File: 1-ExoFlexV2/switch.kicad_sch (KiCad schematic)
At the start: 40 parts, among them J20 SWMAX1, J21 SWMIN1, J22 SWMAX2, J23 SWMIN2, J24 SWMAX3, J25 SWMIN3, J26 SWMAX4, J27 SWMAX5, J28 URG1, J29 RESET

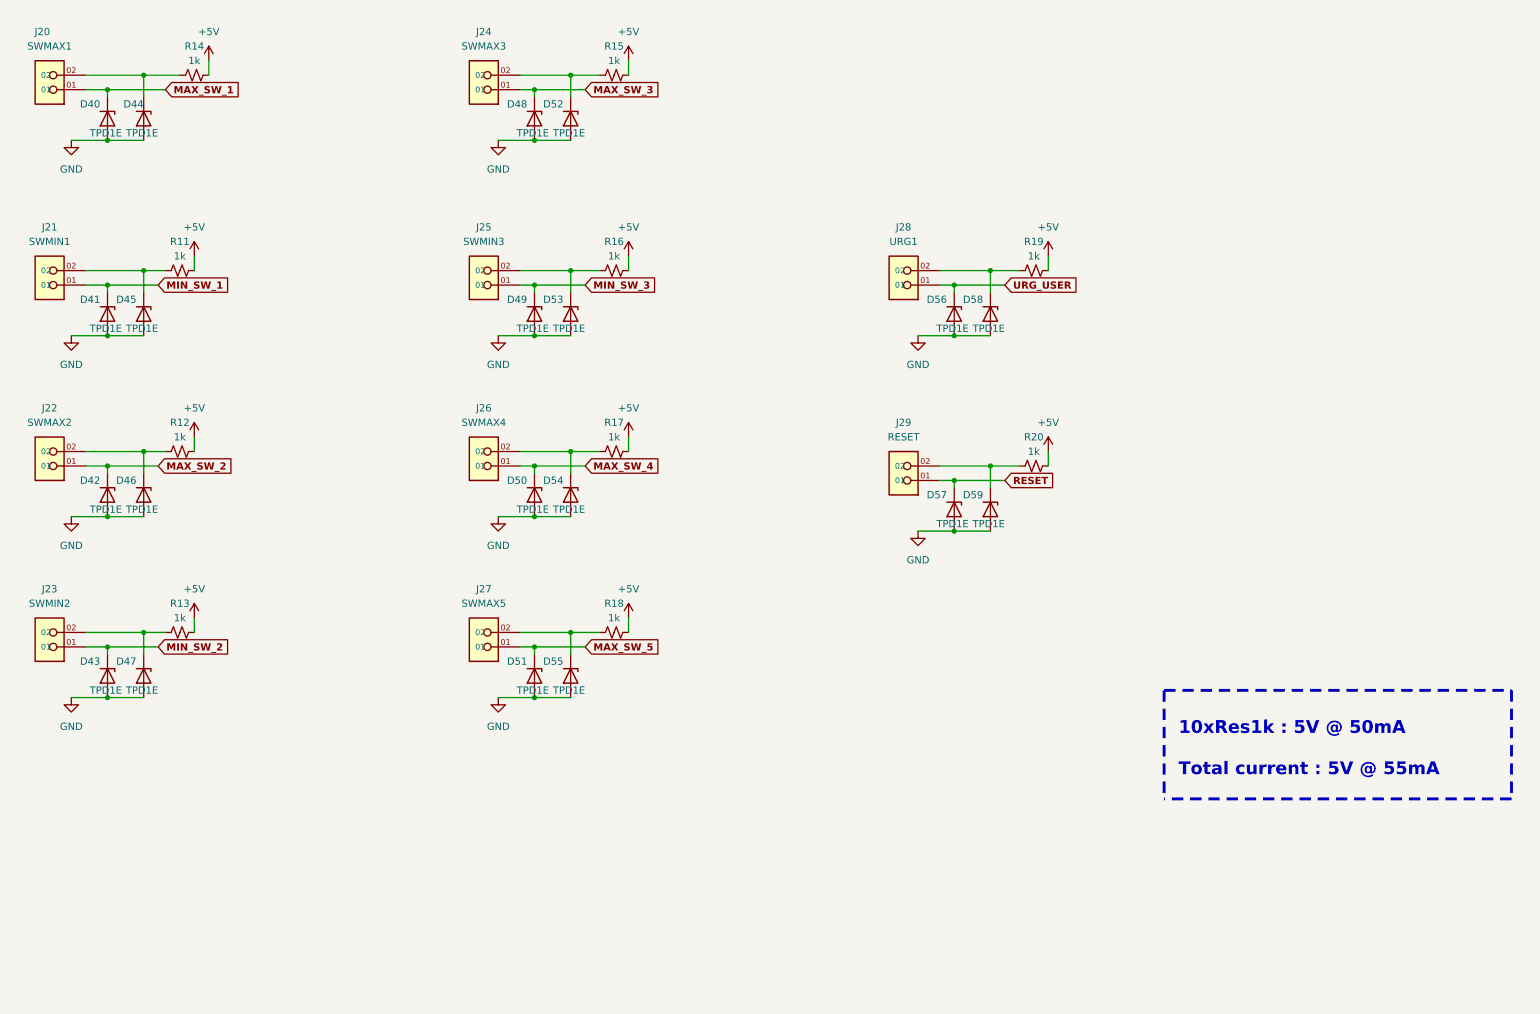
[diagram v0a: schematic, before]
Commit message: Trimmer et jumper
-Changement de symbole de jumper
-Ajout des des trimmer aux endroits nécessaires
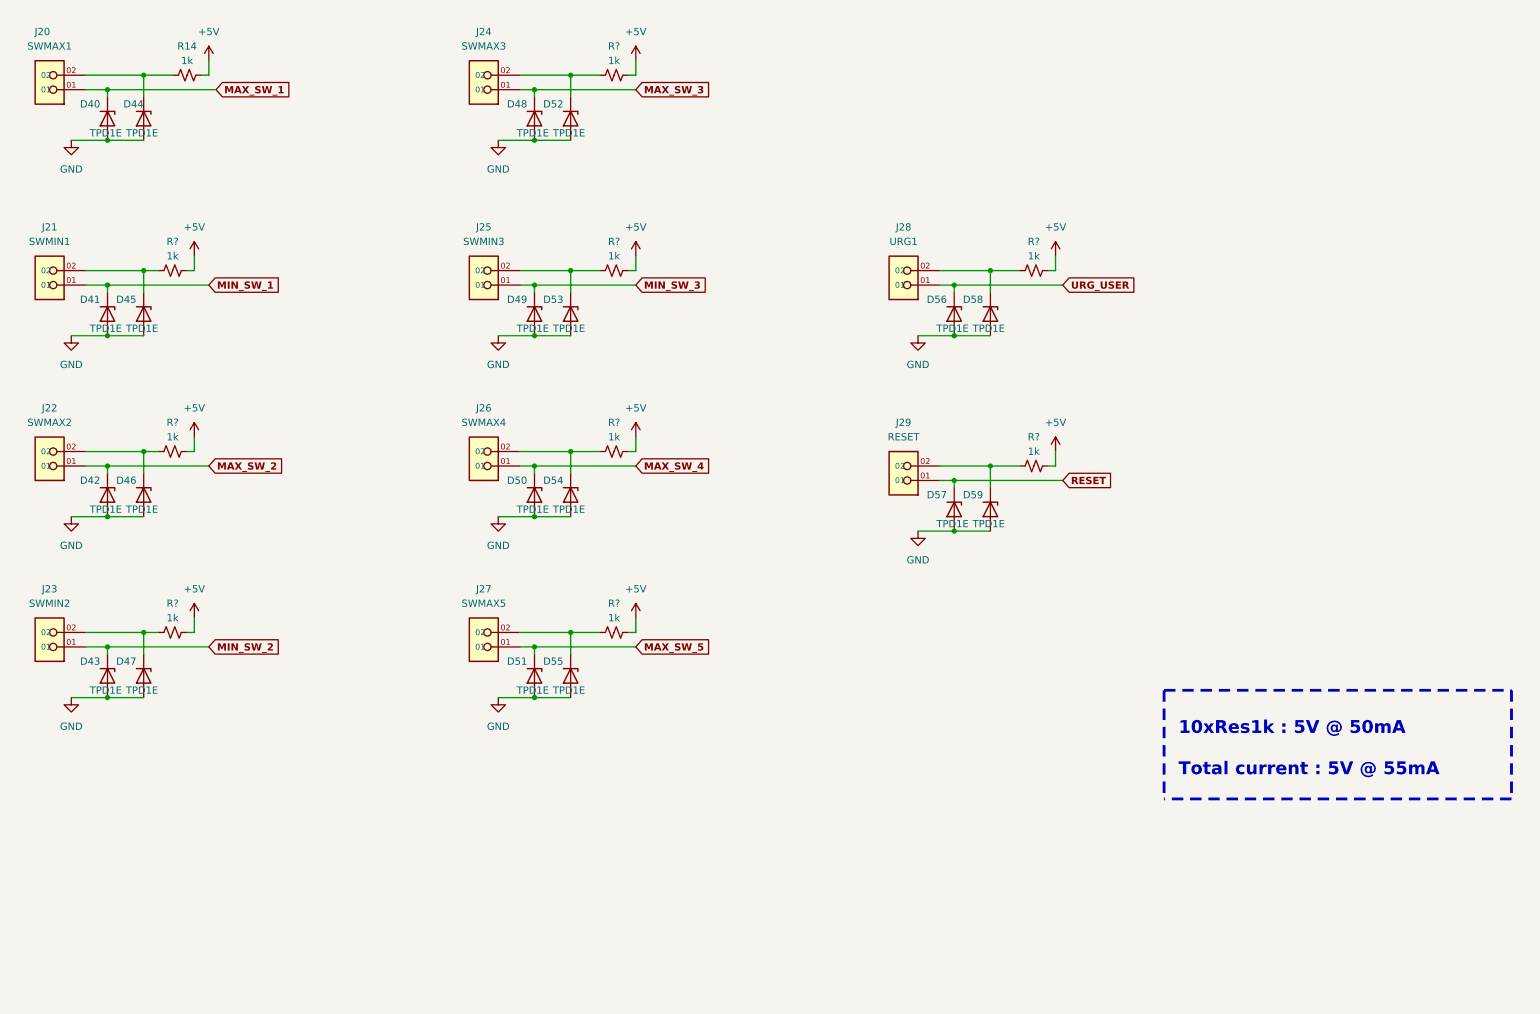
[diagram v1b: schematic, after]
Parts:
- removed R11, R12, R13, R15, R16, R17, R18, R19, R20: 1k, Resistor_SMD:R_0603_1608Metric, symbol Device:R_Small_US
- added R? (x9): 1k, Resistor_SMD:R_0805_2012Metric, symbol Device:R_Small_US
- R14: footprint Resistor_SMD:R_0603_1608Metric -> Resistor_SMD:R_0805_2012Metric
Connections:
- net +5V: now also R?.2, R?.2, R?.2, R?.2, R?.2, R?.2, R?.2, R?.2, R?.2
- net at D53.1 (K), J25.02: now also R?.1
- net at D59.1 (K), J29.02: now also R?.1
- net at D45.1 (K), J21.02: now also R?.1
- net at D47.1 (K), J23.02: now also R?.1
- net at D52.1 (K), J24.02: now also R?.1
- net at D54.1 (K), J26.02: now also R?.1
- net at D58.1 (K), J28.02: now also R?.1
- net at D46.1 (K), J22.02: now also R?.1
- net at D55.1 (K), J27.02: now also R?.1
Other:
- moved on the sheet: R14

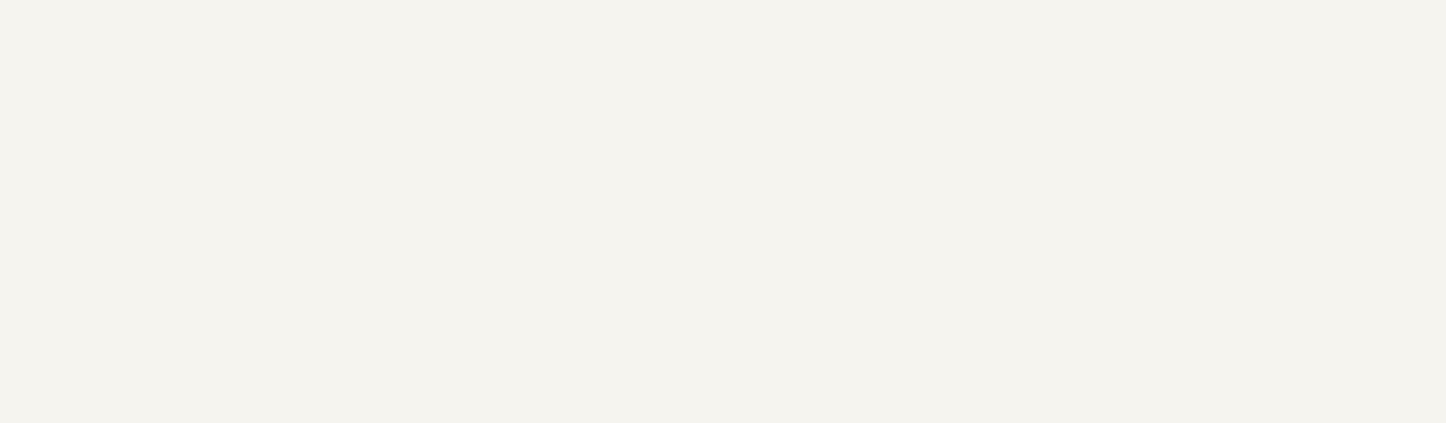
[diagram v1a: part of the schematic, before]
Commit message: Test points et notes
- Ajout de tous les tests point nécessaires
-  Ajoute des sections de notes dans chaque page
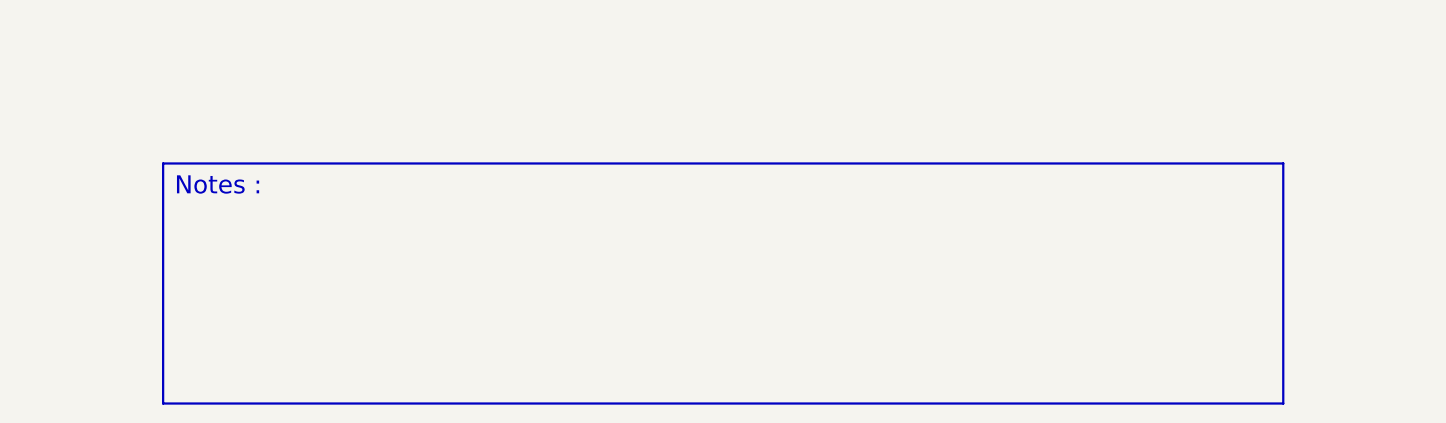
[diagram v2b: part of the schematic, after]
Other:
- note added: "Notes :"
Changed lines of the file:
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@@
     (stroke (width 0) (type default) (color 0 0 0 0))
+  )
+  (polyline (pts (xy 49.53 168.91) (xy 173.99 168.91))
+    (stroke (width 0.25) (type solid) (color 0 0 0 0))
   )
   (wire (pts (xy 40.64 99.06) (xy 40.64 102.87))
@@
     (stroke (width 0) (type default) (color 0 0 0 0))
   )
+  (polyline (pts (xy 173.99 168.91) (xy 173.99 195.58))
+    (stroke (width 0.25) (type solid) (color 0 0 0 0))
+  )
   (wire (pts (xy 109.22 36.83) (xy 109.22 35.56))
     (stroke (width 0) (type default) (color 0 0 0 0))
@@
     (stroke (width 0) (type default) (color 0 0 0 0))
   )
+  (polyline (pts (xy 49.53 168.91) (xy 49.53 195.58))
+    (stroke (width 0.25) (type solid) (color 0 0 0 0))
+  )
   (wire (pts (xy 127 96.52) (xy 127 99.06))
     (stroke (width 0) (type default) (color 0 0 0 0))
@@
   (wire (pts (xy 40.64 130.81) (xy 40.64 134.62))
     (stroke (width 0) (type default) (color 0 0 0 0))
+  )
+  (polyline (pts (xy 173.99 195.58) (xy 49.53 195.58))
+    (stroke (width 0.25) (type solid) (color 0 0 0 0))
   )
   (wire (pts (xy 189.23 67.31) (xy 194.31 67.31))
@@
     (effects (font (size 2.25 2.25) (thickness 0.5) bold) (justify left bottom))
   )
+  (text "Notes :" (at 50.8 172.72 0)
+    (effects (font (size 2 2)) (justify left bottom))
+  )
   (global_label "MAX_SW_1" (shape input) (at 53.34 35.56 0) (fields_autoplaced)

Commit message: Schématisation terminée
- Schéma terminé
- Passage vers le PCB
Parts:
- D39: renamed from D40; value TPD1E -> TVS; DESCRIPTION (none) -> TVS DIODE 5.5VWM 14VC 2X1SON; MANUFACTURER (none) -> Texas Instruments; PACKAGE (none) -> 0402 (1006 Metric); PART NUMBER (none) -> TPD1E05U06DPYR; TYPE (none) -> SMD
- D40: renamed from D41; value TPD1E -> TVS; DESCRIPTION (none) -> TVS DIODE 5.5VWM 14VC 2X1SON; MANUFACTURER (none) -> Texas Instruments; PACKAGE (none) -> 0402 (1006 Metric); PART NUMBER (none) -> TPD1E05U06DPYR; TYPE (none) -> SMD
- D41: renamed from D42; value TPD1E -> TVS; DESCRIPTION (none) -> TVS DIODE 5.5VWM 14VC 2X1SON; MANUFACTURER (none) -> Texas Instruments; PACKAGE (none) -> 0402 (1006 Metric); PART NUMBER (none) -> TPD1E05U06DPYR; TYPE (none) -> SMD
- D42: renamed from D43; value TPD1E -> TVS; DESCRIPTION (none) -> TVS DIODE 5.5VWM 14VC 2X1SON; MANUFACTURER (none) -> Texas Instruments; PACKAGE (none) -> 0402 (1006 Metric); PART NUMBER (none) -> TPD1E05U06DPYR; TYPE (none) -> SMD
- D43: renamed from D44; value TPD1E -> TVS; DESCRIPTION (none) -> TVS DIODE 5.5VWM 14VC 2X1SON; MANUFACTURER (none) -> Texas Instruments; PACKAGE (none) -> 0402 (1006 Metric); PART NUMBER (none) -> TPD1E05U06DPYR; TYPE (none) -> SMD
- D44: renamed from D45; value TPD1E -> TVS; DESCRIPTION (none) -> TVS DIODE 5.5VWM 14VC 2X1SON; MANUFACTURER (none) -> Texas Instruments; PACKAGE (none) -> 0402 (1006 Metric); PART NUMBER (none) -> TPD1E05U06DPYR; TYPE (none) -> SMD
- D45: renamed from D46; value TPD1E -> TVS; DESCRIPTION (none) -> TVS DIODE 5.5VWM 14VC 2X1SON; MANUFACTURER (none) -> Texas Instruments; PACKAGE (none) -> 0402 (1006 Metric); PART NUMBER (none) -> TPD1E05U06DPYR; TYPE (none) -> SMD
- D46: renamed from D47; value TPD1E -> TVS; DESCRIPTION (none) -> TVS DIODE 5.5VWM 14VC 2X1SON; MANUFACTURER (none) -> Texas Instruments; PACKAGE (none) -> 0402 (1006 Metric); PART NUMBER (none) -> TPD1E05U06DPYR; TYPE (none) -> SMD
- D47: renamed from D48; value TPD1E -> TVS; DESCRIPTION (none) -> TVS DIODE 5.5VWM 14VC 2X1SON; MANUFACTURER (none) -> Texas Instruments; PACKAGE (none) -> 0402 (1006 Metric); PART NUMBER (none) -> TPD1E05U06DPYR; TYPE (none) -> SMD
- D48: renamed from D49; value TPD1E -> TVS; DESCRIPTION (none) -> TVS DIODE 5.5VWM 14VC 2X1SON; MANUFACTURER (none) -> Texas Instruments; PACKAGE (none) -> 0402 (1006 Metric); PART NUMBER (none) -> TPD1E05U06DPYR; TYPE (none) -> SMD
- D49: renamed from D50; value TPD1E -> TVS; DESCRIPTION (none) -> TVS DIODE 5.5VWM 14VC 2X1SON; MANUFACTURER (none) -> Texas Instruments; PACKAGE (none) -> 0402 (1006 Metric); PART NUMBER (none) -> TPD1E05U06DPYR; TYPE (none) -> SMD
- D50: renamed from D51; value TPD1E -> TVS; DESCRIPTION (none) -> TVS DIODE 5.5VWM 14VC 2X1SON; MANUFACTURER (none) -> Texas Instruments; PACKAGE (none) -> 0402 (1006 Metric); PART NUMBER (none) -> TPD1E05U06DPYR; TYPE (none) -> SMD
- D51: renamed from D52; value TPD1E -> TVS; DESCRIPTION (none) -> TVS DIODE 5.5VWM 14VC 2X1SON; MANUFACTURER (none) -> Texas Instruments; PACKAGE (none) -> 0402 (1006 Metric); PART NUMBER (none) -> TPD1E05U06DPYR; TYPE (none) -> SMD
- D52: renamed from D53; value TPD1E -> TVS; DESCRIPTION (none) -> TVS DIODE 5.5VWM 14VC 2X1SON; MANUFACTURER (none) -> Texas Instruments; PACKAGE (none) -> 0402 (1006 Metric); PART NUMBER (none) -> TPD1E05U06DPYR; TYPE (none) -> SMD
- D53: renamed from D54; value TPD1E -> TVS; DESCRIPTION (none) -> TVS DIODE 5.5VWM 14VC 2X1SON; MANUFACTURER (none) -> Texas Instruments; PACKAGE (none) -> 0402 (1006 Metric); PART NUMBER (none) -> TPD1E05U06DPYR; TYPE (none) -> SMD
- D54: renamed from D55; value TPD1E -> TVS; DESCRIPTION (none) -> TVS DIODE 5.5VWM 14VC 2X1SON; MANUFACTURER (none) -> Texas Instruments; PACKAGE (none) -> 0402 (1006 Metric); PART NUMBER (none) -> TPD1E05U06DPYR; TYPE (none) -> SMD
- D55: renamed from D56; value TPD1E -> TVS; DESCRIPTION (none) -> TVS DIODE 5.5VWM 14VC 2X1SON; MANUFACTURER (none) -> Texas Instruments; PACKAGE (none) -> 0402 (1006 Metric); PART NUMBER (none) -> TPD1E05U06DPYR; TYPE (none) -> SMD
- D56: renamed from D57; value TPD1E -> TVS; DESCRIPTION (none) -> TVS DIODE 5.5VWM 14VC 2X1SON; MANUFACTURER (none) -> Texas Instruments; PACKAGE (none) -> 0402 (1006 Metric); PART NUMBER (none) -> TPD1E05U06DPYR; TYPE (none) -> SMD
- D57: renamed from D58; value TPD1E -> TVS; DESCRIPTION (none) -> TVS DIODE 5.5VWM 14VC 2X1SON; MANUFACTURER (none) -> Texas Instruments; PACKAGE (none) -> 0402 (1006 Metric); PART NUMBER (none) -> TPD1E05U06DPYR; TYPE (none) -> SMD
- D58: renamed from D59; value TPD1E -> TVS; DESCRIPTION (none) -> TVS DIODE 5.5VWM 14VC 2X1SON; MANUFACTURER (none) -> Texas Instruments; PACKAGE (none) -> 0402 (1006 Metric); PART NUMBER (none) -> TPD1E05U06DPYR; TYPE (none) -> SMD
- J25: renamed from J20; value SWMAX1 -> 2; DESCRIPTION (none) -> 2 Position Wire to Board Terminal Block 55° (125°) Angle wi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; PACKAGE (none) -> 2 POS 0.100" (2.54mm); PART NUMBER (none) -> 1751099; TYPE (none) -> Through Hole
- J26: renamed from J21; value SWMIN1 -> 2; DESCRIPTION (none) -> 2 Position Wire to Board Terminal Block 55° (125°) Angle wi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; PACKAGE (none) -> 2 POS 0.100" (2.54mm); PART NUMBER (none) -> 1751099; TYPE (none) -> Through Hole
- J27: renamed from J22; value SWMAX2 -> 2; DESCRIPTION (none) -> 2 Position Wire to Board Terminal Block 55° (125°) Angle wi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; PACKAGE (none) -> 2 POS 0.100" (2.54mm); PART NUMBER (none) -> 1751099; TYPE (none) -> Through Hole
- J28: renamed from J23; value SWMIN2 -> 2; DESCRIPTION (none) -> 2 Position Wire to Board Terminal Block 55° (125°) Angle wi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; PACKAGE (none) -> 2 POS 0.100" (2.54mm); PART NUMBER (none) -> 1751099; TYPE (none) -> Through Hole
- J29: renamed from J24; value SWMAX3 -> 2; DESCRIPTION (none) -> 2 Position Wire to Board Terminal Block 55° (125°) Angle wi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; PACKAGE (none) -> 2 POS 0.100" (2.54mm); PART NUMBER (none) -> 1751099; TYPE (none) -> Through Hole
- J30: renamed from J25; value SWMIN3 -> 2; DESCRIPTION (none) -> 2 Position Wire to Board Terminal Block 55° (125°) Angle wi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; PACKAGE (none) -> 2 POS 0.100" (2.54mm); PART NUMBER (none) -> 1751099; TYPE (none) -> Through Hole
- J31: renamed from J26; value SWMAX4 -> 2; DESCRIPTION (none) -> 2 Position Wire to Board Terminal Block 55° (125°) Angle wi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; PACKAGE (none) -> 2 POS 0.100" (2.54mm); PART NUMBER (none) -> 1751099; TYPE (none) -> Through Hole
- J32: renamed from J27; value SWMAX5 -> 2; DESCRIPTION (none) -> 2 Position Wire to Board Terminal Block 55° (125°) Angle wi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; PACKAGE (none) -> 2 POS 0.100" (2.54mm); PART NUMBER (none) -> 1751099; TYPE (none) -> Through Hole
- J33: renamed from J28; value URG1 -> 2; DESCRIPTION (none) -> 2 Position Wire to Board Terminal Block 55° (125°) Angle wi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; PACKAGE (none) -> 2 POS 0.100" (2.54mm); PART NUMBER (none) -> 1751099; TYPE (none) -> Through Hole
- J34: renamed from J29; value RESET -> 2; DESCRIPTION (none) -> 2 Position Wire to Board Terminal Block 55° (125°) Angle wi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; PACKAGE (none) -> 2 POS 0.100" (2.54mm); PART NUMBER (none) -> 1751099; TYPE (none) -> Through Hole
- R11, R12, R13, R15, R16, R17, R18, R19, R20: renamed from R?; value 1k -> 1k 1% 1/10W; footprint Resistor_SMD:R_0805_2012Metric -> Resistor_SMD:R_0402_1005Metric; DESCRIPTION (none) -> 1 kOhms ±1% 0.1W, 1/10W Chip Resistor 0402 (1005 Metric) Au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; MANUFACTURER (none) -> Panasonic Electronic Components; PACKAGE (none) -> 0402 (1005 Metric); PART NUMBER (none) -> ERJ-2RKF1001X; TYPE (none) -> SMD
- R14: value 1k -> 1k 1% 1/10W; footprint Resistor_SMD:R_0805_2012Metric -> Resistor_SMD:R_0402_1005Metric; DESCRIPTION (none) -> 1 kOhms ±1% 0.1W, 1/10W Chip Resistor 0402 (1005 Metric) Au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; MANUFACTURER (none) -> Panasonic Electronic Components; PACKAGE (none) -> 0402 (1005 Metric); PART NUMBER (none) -> ERJ-2RKF1001X; TYPE (none) -> SMD
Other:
- note added: "RESET"
- note added: "SWMAX1"
- note added: "SWMAX2"
- note added: "SWMAX3"
- note added: "SWMAX4"
- note added: "SWMAX5"
- note added: "SWMIN1"
- note added: "SWMIN2"
- note added: "SWMIN3"
- note added: "URG1"
